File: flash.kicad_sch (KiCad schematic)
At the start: 5 parts, among them J5 Conn_01x02, U4 W25Q128JVS

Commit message: Complete power regulator schematics
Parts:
- J5: footprint (none) -> Resistor_SMD:R_0402_1005Metric
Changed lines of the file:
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@@
 			)
 		)
-		(property "Footprint" ""
+		(property "Footprint" "Resistor_SMD:R_0402_1005Metric"
 			(at 123.19 81.28 0)
 			(effects

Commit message: Update footprints, route switching regulator circuit block
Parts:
- U4: footprint (none) -> Package_SO:SOIC-8_5.23x5.23mm_P1.27mm
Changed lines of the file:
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@@
 			)
 		)
-		(property "Footprint" ""
+		(property "Footprint" "Package_SO:SOIC-8_5.23x5.23mm_P1.27mm"
 			(at 165.1 132.08 0)
 			(effects

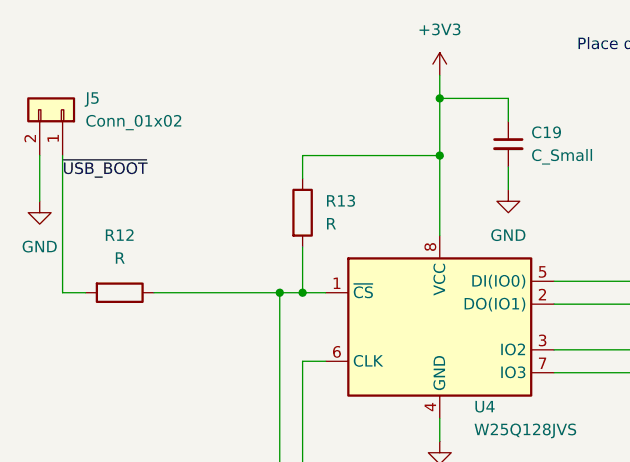
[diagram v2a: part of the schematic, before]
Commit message: Update footprints, route more circuit blocks
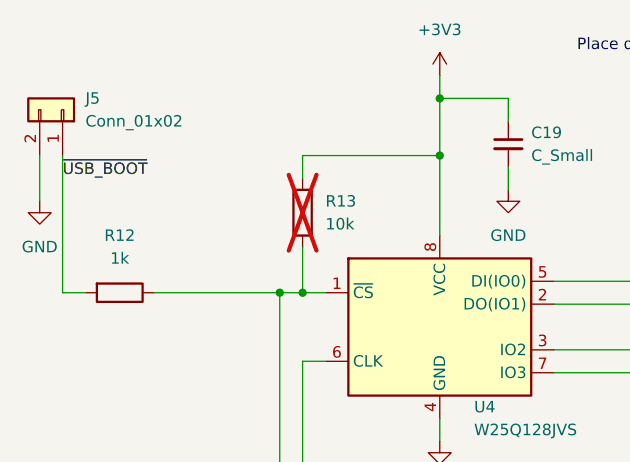
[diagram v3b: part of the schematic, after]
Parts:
- J5: footprint Resistor_SMD:R_0402_1005Metric -> Connector_PinHeader_2.54mm:PinHeader_1x02_P2.54mm_Horizontal
- R12: value R -> 1k
- R13: value R -> 10k; now not fitted
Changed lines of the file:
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@@
 		(fields_autoplaced yes)
 		(property "Reference" "J5"
-			(at 125.73 80.01 90)
+			(at 125.73 80.0099 90)
 			(effects
 				(font
@@
 		)
 		(property "Value" "Conn_01x02"
-			(at 125.73 82.55 90)
+			(at 125.73 82.5499 90)
 			(effects
 				(font
@@
 			)
 		)
-		(property "Footprint" "Resistor_SMD:R_0402_1005Metric"
+		(property "Footprint" "Connector_PinHeader_2.54mm:PinHeader_1x02_P2.54mm_Horizontal"
 			(at 123.19 81.28 0)
 			(effects
@@
 			)
 		)
-		(property "Value" "R"
+		(property "Value" "1k"
 			(at 129.54 97.79 90)
 			(effects
@@
 		(in_bom yes)
 		(on_board yes)
-		(dnp no)
+		(dnp yes)
 		(fields_autoplaced yes)
 		(property "Reference" "R13"
-			(at 152.4 91.44 0)
+			(at 152.4 91.4399 0)
 			(effects
 				(font
@@
 			)
 		)
-		(property "Value" "R"
-			(at 152.4 93.98 0)
-			(effects
-				(font
+		(property "Value" "10k"
+			(at 152.4 93.9799 0)
+			(effects
+				(font

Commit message: Big update, bad commit messsage :)
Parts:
- C701: renamed from C19; footprint Capacitor_SMD:C_0402_1005Metric -> cubesat_rp2040:C_0402_1005Metric
- R701: renamed from R12; footprint Resistor_SMD:R_0402_1005Metric -> cubesat_rp2040:R_0402_1005Metric
- R702: renamed from R13; footprint Resistor_SMD:R_0402_1005Metric -> cubesat_rp2040:R_0402_1005Metric
- renumbered J5 to J701, U4 to U701
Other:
- company: (none) -> Magnus Oksbøl Therkelsen
- title: (none) -> CubeSat RP2040 Board
- moved on the sheet: C701, J701, R701, R702, U701

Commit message: Major update, everything has been touched
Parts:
- removed C701: C_Small, cubesat_rp2040:C_0402_1005Metric, symbol Device:C_Small
- removed J701: Conn_01x02, Connector_PinHeader_2.54mm:PinHeader_1x02_P2.54mm_Horizontal, symbol Connector_Generic:Conn_01x02
- removed R701: 1k, cubesat_rp2040:R_0402_1005Metric, symbol Device:R
- removed R702: 10k, cubesat_rp2040:R_0402_1005Metric, symbol Device:R
- removed U701: W25Q128JVS, Package_SO:SOIC-8_5.23x5.23mm_P1.27mm, symbol cubesat_rp2040:W25Q128JVS
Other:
- note removed: "Place decoupling caps near VCC"
